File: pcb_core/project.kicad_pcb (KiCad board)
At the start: 2 copper layers, 212.3 x 91.7 mm, 145 parts, among them IC1 DRV8871DDA, IC10 DRV8871DDA, IC11 DRV8871DDA, IC12 DRV8871DDA, IC13 DRV8871DDA, IC14 DRV8871DDA, IC15 DRV8871DDA, IC16 DRV8871DDA, IC17 DRV8871DDA, IC18 DRV8871DDA, IC19 SX1509QBIULTRT, IC2 SX1509QBIULTRT, IC20 SI4214DDY-T1-GE3, IC3 DRV8871DDA, IC4 TCA9548APWR, IC5 DRV8871DDA, IC6 DRV8871DDA, IC7 DRV8871DDA, IC8 DRV8871DDA, IC9 DRV8871DDA, J1 Conn_01x02, J10 1053131103, J11 1053131103, J12 1053131103, J13 1053131103, J14 1053131103, J15 1053131103, J16 1053131103, J17 1053131103, J18 1053131103, J19 Conn_02x02_Counter_Clockwise, J2 1725656, J20 PCBConnector, J21 PCBConnector, J22 PCBConnector, J23 PCBConnector, J25 PCBConnector, J27 PCBConnector, J3 1053131103, J4 1053131103, J5 1053131103, J6 1053131103, J7 1053131103, J8 1053131103, J9 1053131103, U1 ESP32-S3-WROOM-2, U2 LTC4365TS8, U3 ESP32-DevKitC

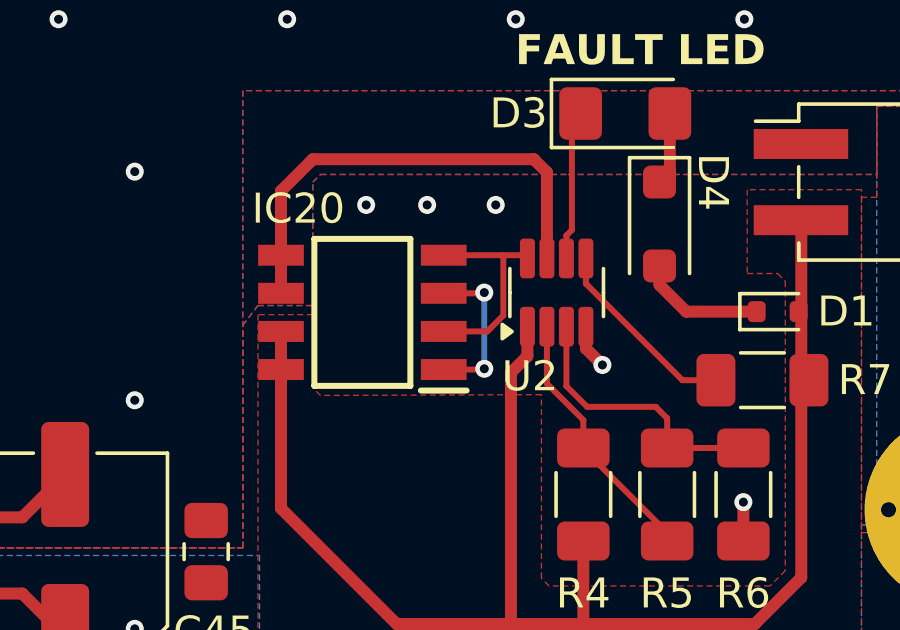
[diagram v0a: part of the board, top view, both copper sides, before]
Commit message: Optimize PCB to reduce vias
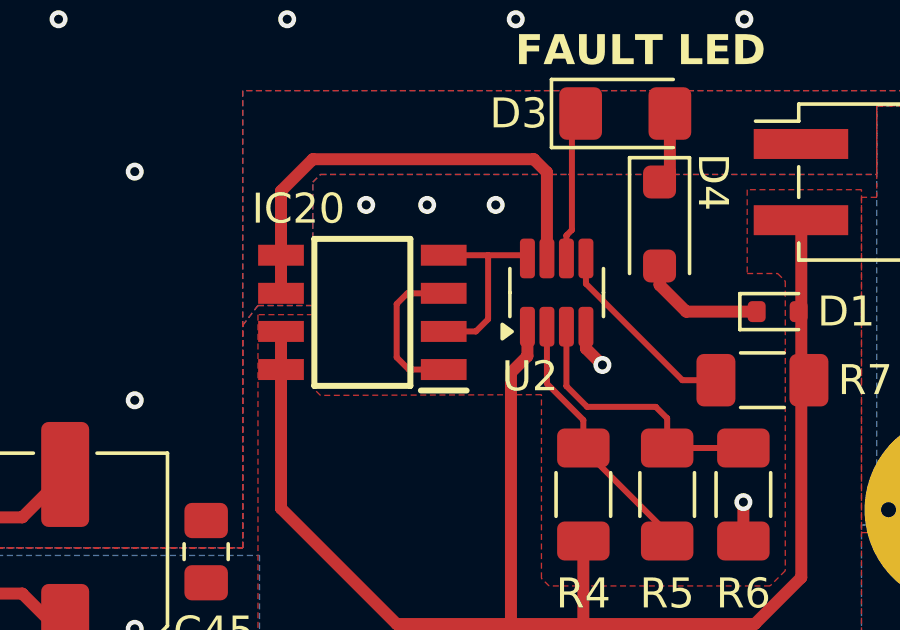
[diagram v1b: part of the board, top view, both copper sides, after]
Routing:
- net Net-(IC20-S1): track 5.19 -> 5.23 mm, vias 2 -> 0
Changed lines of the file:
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@@
 	)
 	(segment
-		(start 233.426 116.713)
-		(end 233.426 114.7064)
+		(start 232.918 116.84)
+		(end 232.918 114.7064)
 		(width 0.2)
 		(layer "F.Cu")
@@
 	)
 	(segment
-		(start 231.439 117.2464)
-		(end 232.8926 117.2464)
-		(width 0.2)
-		(layer "F.Cu")
-		(net 48)
-	)
-	(segment
-		(start 232.8926 117.2464)
-		(end 233.426 116.713)
+		(start 232.5116 117.2464)
+		(end 232.918 116.84)
 		(width 0.2)
 		(layer "F.Cu")
@@
 	)
 	(segment
-		(start 231.439 115.9764)
-		(end 232.7656 115.9764)
+		(start 231.439 117.2464)
+		(end 232.5116 117.2464)
+		(width 0.2)
+		(layer "F.Cu")
+		(net 48)
+	)
+	(segment
+		(start 230.2256 115.9764)
+		(end 229.87 116.332)
 		(width 0.2)
 		(layer "F.Cu")
@@
 	)
 	(segment
-		(start 231.439 118.5164)
-		(end 232.7656 118.5164)
+		(start 231.439 115.9764)
+		(end 230.2256 115.9764)
 		(width 0.2)
 		(layer "F.Cu")
 		(net 49)
 	)
-	(via
-		(at 232.791 118.491)
-		(size 0.6)
-		(drill 0.3)
-		(layers "F.Cu" "B.Cu")
-		(net 49)
-	)
-	(via
-		(at 232.791 115.951)
-		(size 0.6)
-		(drill 0.3)
-		(layers "F.Cu" "B.Cu")
+	(segment
+		(start 230.2764 118.5164)
+		(end 231.439 118.5164)
+		(width 0.2)
+		(layer "F.Cu")
 		(net 49)
 	)
 	(segment
-		(start 232.791 118.491)
-		(end 232.791 115.951)
+		(start 229.87 118.11)
+		(end 230.2764 118.5164)
 		(width 0.2)
-		(layer "B.Cu")
+		(layer "F.Cu")
 		(net 49)
 	)
+	(segment
+		(start 229.87 116.332)
+		(end 229.87 118.11)
+		(width 0.2)
+		(layer "F.Cu")
+		(net 49)
+	)

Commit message: Optimize PCB
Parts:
- moved J2 0.13 mm to (254.8, 122.9)
- moved J21 0.13 mm to (258.1, 116.3)
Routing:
- net GNDA: vias 367 -> 366
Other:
- outline, holes or cut-outs redrawn

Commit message: New package version of model train controller
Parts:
- removed C1, C11: 10uF, Capacitor_SMD:C_1206_3216Metric_Pad1.33x1.80mm_HandSolder
- removed C2, C3, C4: 0.1uF, Capacitor_SMD:C_1206_3216Metric_Pad1.33x1.80mm_HandSolder
- removed C43, C44, C8, C9: 0.1uF, Capacitor_SMD:C_0805_2012Metric_Pad1.18x1.45mm_HandSolder
- removed C45: 4.7uF, Capacitor_SMD:C_0805_2012Metric_Pad1.18x1.45mm_HandSolder
- removed C5: 1uF, Capacitor_SMD:C_1206_3216Metric_Pad1.33x1.80mm_HandSolder
- removed D1: 1N4148WT, Diode_SMD:D_SOD-523
- removed D3: RED LED, LED_SMD:LED_1206_3216Metric_Pad1.42x1.75mm_HandSolder
- removed D4: ~, Diode_SMD:D_SOD-123F
- removed IC19, IC2: SX1509QBIULTRT, library:QFN40P400X400X60-29N-D
- removed IC20: SI4214DDY-T1-GE3, library:SOIC127P600X175-8N
- removed IC4: TCA9548APWR, library:SOP65P640X120-24N
- removed J19: Conn_02x02_Counter_Clockwise, Connector_PinHeader_2.54mm:PinHeader_2x02_P2.54mm_Vertical_SMD
- removed J23: PCBConnector, TestPoint:TestPoint_THTPad_D3.0mm_Drill1.5mm
- removed R10, R11, R12, R16, R2, R9: 10k, Resistor_SMD:R_1206_3216Metric_Pad1.30x1.75mm_HandSolder
- removed R13, R14, R15, R17, R19, R20: 5k, Resistor_SMD:R_1206_3216Metric_Pad1.30x1.75mm_HandSolder
- removed R3: 0, Resistor_SMD:R_1206_3216Metric_Pad1.30x1.75mm_HandSolder
- removed R4: 250k, Resistor_SMD:R_1206_3216Metric_Pad1.30x1.75mm_HandSolder
- removed R5: 40.2k, Resistor_SMD:R_1206_3216Metric_Pad1.30x1.75mm_HandSolder
- removed R6: 13M, Resistor_SMD:R_1206_3216Metric_Pad1.30x1.75mm_HandSolder
- removed R7: 510k, Resistor_SMD:R_1206_3216Metric_Pad1.30x1.75mm_HandSolder
- removed S1, S2: EVP-3AA02Q, library:EVP3AA02Q
- removed S3: A6S-3102-PH, library:A6S3102PH
- removed U3: ESP32-DevKitC, PCM_Espressif:ESP32-DevKitC
- added U4: ~, cust_pcb:ioexpander, F.Cu at (175.5, 93.6)
- added U5: ~, cust_pcb:ioexpander, F.Cu at (87.4, 98.1)
- added U6: ~, cust_pcb:i2cmultiplexer, F.Cu at (117.3, 117.6)
- J1: value Conn_01x02 -> PCBConnector; footprint Connector_PinHeader_2.54mm:PinHeader_1x02_P2.54mm_Vertical -> TestPoint:TestPoint_THTPad_D3.0mm_Drill1.5mm
- U1: value ESP32-S3-WROOM-2 -> ~; footprint PCM_Espressif:ESP32-S3-WROOM-2 -> cust_pcb:esp32
- U2: value LTC4365TS8 -> ~; footprint Package_TO_SOT_SMD:TSOT-23-8 -> cust_pcb:voltage_protection
- moved J22 20.3 mm to (141.5, 128.8)
- moved J20 15.7 mm to (253.2, 100.6)
- moved J21 15.7 mm to (258.1, 100.6)
- moved J1 10.2 mm to (141.5, 123.7), turned to 0 degrees
- moved U2 8.44 mm to (233.4, 124.2), turned to 0 degrees
- moved U1 8.17 mm to (172.5, 116.1), turned to 0 degrees
- moved H6 2.54 mm to (154.9, 86.4)
- moved H7 2.54 mm to (154.9, 127.5)
- moved C42 0.28 mm to (218.7, 124.5), turned to -90 degrees
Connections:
- C42 pad 1: GNDA -> PROD_24V
- C42 pad 2: PROD_24V -> GNDA
- J1 pad 1: ESP32_TX -> ESP32_SCL
- J20 pad 1: /24V -> PROD_24V
- U1 pad 1: GNDD -> ESP32_SDA
- U1 pad 10: unconnected-(U1-GPIO17/U1TXD/ADC2_CH6-Pad10) -> GNDD
- U1 pad 11: unconnected-(U1-GPIO18/U1RXD/ADC2_CH7/CLK_OUT3-Pad11) -> GNDD
- U1 pad 12: unconnected-(U1-GPIO8/TOUCH8/ADC1_CH7/SUBSPICS1-Pad12) -> GNDD
- U1 pad 13: unconnected-(U1-GPIO19/U1RTS/ADC2_CH8/CLK_OUT2/USB_D--Pad13) -> GNDD
- U1 pad 14: unconnected-(U1-GPIO20/U1CTS/ADC2_CH9/CLK_OUT1/USB_D+-Pad14) -> GNDD
- U1 pad 15: unconnected-(U1-GPIO3/TOUCH3/ADC1_CH2-Pad15) -> GNDD
- U1 pad 16: unconnected-(U1-GPIO46-Pad16) -> GNDD
- U1 pad 17: unconnected-(U1-GPIO9/TOUCH9/ADC1_CH8/FSPIHD/SUBSPIHD-Pad17) -> GNDD
- U1 pad 18: unconnected-(U1-GPIO10/TOUCH10/ADC1_CH9/FSPICS0/FSPIIO4/SUBSPICS0-Pad18) -> VCC_3V3
- U1 pad 2: Net-(U1-3V3) -> ESP32_SCL
- U1 pad 3: /ESP32_EN -> GNDD
- U1 pad 4: unconnected-(U1-GPIO4/TOUCH4/ADC1_CH3-Pad4) -> GNDD
- U1 pad 5: unconnected-(U1-GPIO5/TOUCH5/ADC1_CH4-Pad5) -> GNDD
- U1 pad 6: unconnected-(U1-GPIO6/TOUCH6/ADC1_CH5-Pad6) -> GNDD
- U1 pad 7: unconnected-(U1-GPIO7/TOUCH7/ADC1_CH6-Pad7) -> GNDD
- U1 pad 8: unconnected-(U1-GPIO15/U0RTS/ADC2_CH4/XTAL_32K_P-Pad8) -> GNDD
- U1 pad 9: unconnected-(U1-GPIO16/U0CTS/ADC2_CH5/XTAL_32K_N-Pad9) -> GNDD
- U2 pad 1: VIN_24V -> GNDA
- U2 pad 2: Net-(U2-UV) -> GNDA
- U2 pad 3: Net-(U2-OV) -> GNDA
- U2 pad 4: GNDA -> PROD_24V
- U2 pad 5: Net-(U2-~{SHDN}) -> PROD_24V
- U2 pad 6: Net-(D3-K) -> PROD_24V
- U2 pad 7: PROD_24V -> /24V
- U2 pad 8: Net-(IC20-G1) -> /24V
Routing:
- net VCC_3V3: track 365.5 -> 167.9 mm, vias 20 -> 11
- net ESP32_TX: track 127.7 -> 0.00 mm
- net ESP32_RX: track 124.0 -> 0.00 mm
- net ESP32_SCL: track 124.4 -> 40.3 mm
- net ESP32_SDA: track 120.2 -> 42.4 mm, vias 1 -> 0
- net GNDD: track 64.9 -> 0.04 mm, vias 369 -> 354
- net VIN_24V: track 50.3 -> 0.00 mm
- net /ESP32_EN: track 42.6 -> 0.00 mm, vias 2 -> 0
- net IN2_13: track 14.5 -> 51.8 mm
- net IN1_13: track 14.9 -> 51.2 mm
- net IN2_14: track 24.2 -> 57.9 mm
- net IN1_14: track 25.6 -> 57.4 mm
- net IN2_9: track 43.7 -> 13.2 mm
- net IN1_9: track 41.5 -> 14.3 mm
- net IOEXP01_SCL: track 74.4 -> 49.0 mm, vias 2 -> 0
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- removed copper zone on F.Cu, net VIN_24V
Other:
- board text removed: "0x70 OFF OFF OFF 0x71 OFF OFF ON 0x72 OFF ON OFF 0x73 OFF ON ON 0x74 ON OFF OFF 0x75 ON OFF ON 0x76 ON ON OFF 0x77 ON ON ON"
- board text removed: "================"
- board text removed: "A0"
- board text removed: "A1"
- board text removed: "A2"
- board text removed: "ADDR A2 A1 A0"
- board text removed: "BOOT"
- board text removed: "Direct"
- board text removed: "FAULT LED"
- board text removed: "I²C Addresses:"
- board text removed: "I²C: 0x3E"
- board text removed: "Protected"
- board text removed: "RESET"
- board text removed: "RX"
- board text removed: "TX"
- board text removed: "UART"

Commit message: Add Panelize connector to PCB_Core
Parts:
- added T1: Tab, PCM_kikit:Tab, F.Cu at (61.0, 133.1)
- added T2: Tab, PCM_kikit:Tab, F.Cu at (157.5, 133.1)
- added T3: Tab, PCM_kikit:Tab, F.Cu at (247.9, 133.1)
- added T4: Tab, PCM_kikit:Tab, F.Cu at (47.8, 86.4)
- added T5: Tab, PCM_kikit:Tab, F.Cu at (261.1, 86.4)
- added T6: Tab, PCM_kikit:Tab, F.Cu at (61.0, 39.9)
- added T7: Tab, PCM_kikit:Tab, F.Cu at (157.5, 39.9)
- added T8: Tab, PCM_kikit:Tab, F.Cu at (247.9, 39.9)

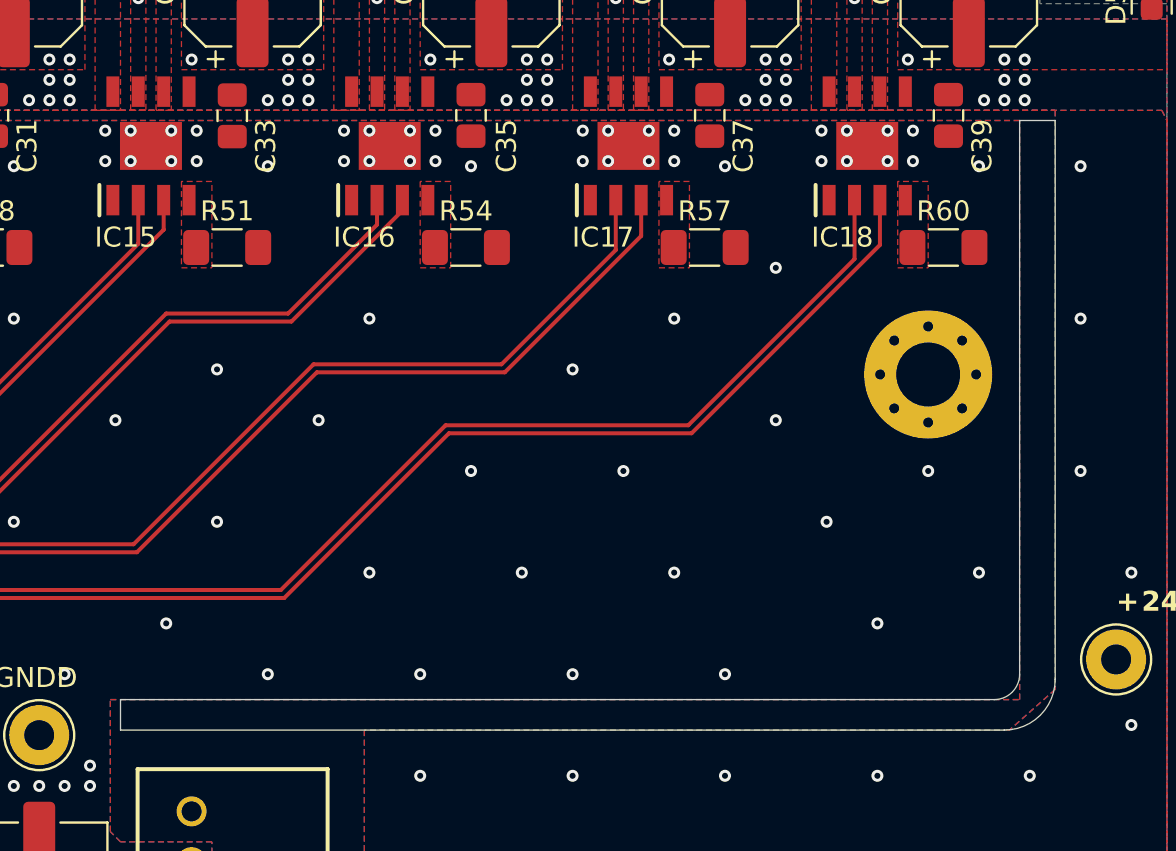
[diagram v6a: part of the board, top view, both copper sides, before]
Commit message: Optimize cutout rounding
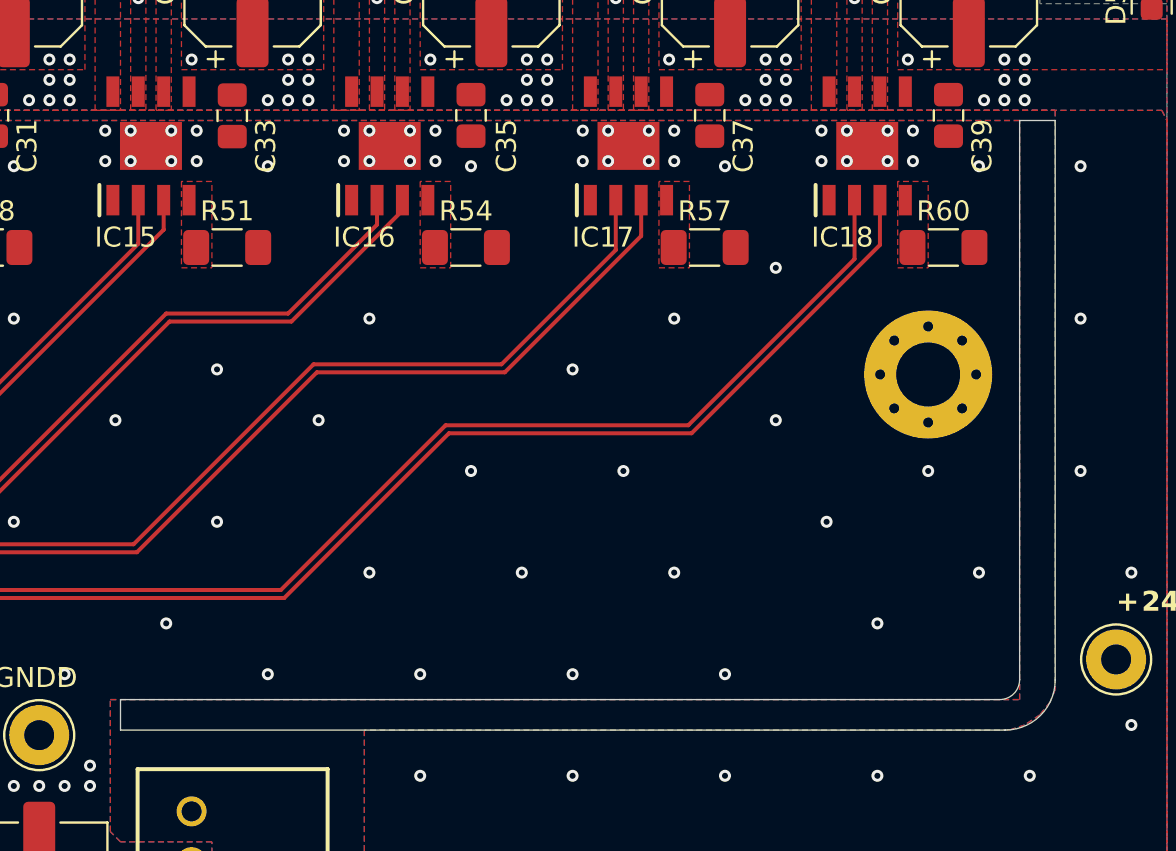
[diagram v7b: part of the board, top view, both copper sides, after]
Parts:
- moved T6 0.51 mm to (61.0, 40.4)
- moved T7 0.51 mm to (157.5, 40.4)
- moved T8 0.51 mm to (247.9, 40.4)
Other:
- outline, holes or cut-outs redrawn
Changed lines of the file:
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@@
 	(footprint "PCM_kikit:Tab"
 		(layer "F.Cu")
-		(at 157.48 39.878 -90)
+		(at 157.48 40.386 -90)
 		(descr "A symbol representing annotation for tab placement")
 		(property "Reference" "T7"
@@
 		)
 		(fp_text user "KIKIT: width: 3mm"
-			(at -5.5 0 360)
+			(at -5.5 0 0)
 			(layer "Dwgs.User")
 			(effects
@@
 		)
 		(fp_text user "KIKIT: width: 3mm"
-			(at -5.5 0 360)
+			(at -5.5 0 0)
 			(layer "Dwgs.User")
 			(effects
@@
 	(footprint "PCM_kikit:Tab"
 		(layer "F.Cu")
-		(at 60.96 39.878 -90)
+		(at 60.96 40.386 -90)
 		(descr "A symbol representing annotation for tab placement")
 		(property "Reference" "T6"
@@
 		)
 		(fp_text user "KIKIT: width: 3mm"
-			(at -5.5 0 360)
+			(at -5.5 0 0)
 			(layer "Dwgs.User")
 			(effects
@@
 		(descr "A symbol representing annotation for tab placement")
 		(property "Reference" "T5"
-			(at 0 -2 360)
+			(at 0 -2 0)
 			(layer "F.SilkS")
 			(hide yes)
@@
 		)
 		(property "Value" "Tab"
-			(at -2.75 -1 360)
+			(at -2.75 -1 0)
 			(layer "Dwgs.User")
 			(effects
@@
 		)
 		(property "Footprint" "PCM_kikit:Tab"
-			(at 0 0 360)
+			(at 0 0 0)
 			(layer "F.Fab")
 			(hide yes)
@@
 		)
 		(property "Datasheet" ""
-			(at 0 0 360)
+			(at 0 0 0)
 			(layer "F.Fab")
 			(hide yes)
@@
 		)
 		(property "Description" "KiKit tab annotations"
-			(at 0 0 360)
+			(at 0 0 0)
 			(layer "F.Fab")
 			(hide yes)
@@
 		)
 		(fp_text user "KIKIT: width: 3mm"
-			(at -5.5 0 360)
+			(at -5.5 0 0)
 			(layer "Dwgs.User")
 			(effects
@@
 		)
 		(fp_text user "KIKIT: width: 3mm"
-			(at -5.5 0 360)
+			(at -5.5 0 0)
 			(layer "Dwgs.User")
 			(effects
@@
 	(footprint "PCM_kikit:Tab"
 		(layer "F.Cu")
-		(at 247.904 39.878 -90)
+		(at 247.904 40.386 -90)
 		(descr "A symbol representing annotation for tab placement")
 		(property "Reference" "T8"
@@
 		)
 		(fp_text user "KIKIT: width: 3mm"
-			(at -5.5 0 360)
+			(at -5.5 0 0)
 			(layer "Dwgs.User")
 			(effects
@@
 		(layer "Edge.Cuts")
 	)
-	(gr_arc
-		(start 248.412 101.346)
-		(mid 248.040026 102.244025)
-		(end 247.142001 102.615999)
-		(stroke
-			(width 0.05)
-			(type default)
-		)
-		(layer "Edge.Cuts")
-	)
 	(gr_rect
 		(start 258.318 127.508)
@@
 		(layer "Edge.Cuts")
 	)
+	(gr_arc
+		(start 248.412 101.616)
+		(mid 248.119107 102.323107)
+		(end 247.412 102.616)
+		(stroke
+			(width 0.05)
+			(type default)
+		)
+		(layer "Edge.Cuts")
+	)
 	(gr_line
-		(start 247.65 104.14)
+		(start 247.69 104.14)
 		(end 203.454 104.14)
 		(stroke
@@
 	(gr_line
 		(start 248.412 73.66)
-		(end 248.412 101.346)
+		(end 248.412 101.616)
 		(stroke
 			(width 0.05)
@@
 	(gr_line
 		(start 203.454 102.616)
-		(end 247.142001 102.615999)
+		(end 247.412 102.616)
 		(stroke
 			(width 0.05)
@@
 		(layer "Edge.Cuts")
 	)
-	(gr_arc
-		(start 250.19 101.6)
-		(mid 249.446051 103.396051)
-		(end 247.65 104.14)
+	(gr_line
+		(start 250.19 73.66)
+		(end 250.19 101.64)
 		(stroke
 			(width 0.05)
@@
 		(layer "Edge.Cuts")
 	)
-	(gr_line
-		(start 250.19 73.66)
-		(end 250.19 101.6)
+	(gr_arc
+		(start 250.19 101.64)
+		(mid 249.457767 103.407767)
+		(end 247.69 104.14)
 		(stroke
 			(width 0.05)
@@
 		(polygon
 			(pts
-				(xy 58.928 68.58) (xy 58.928 73.152) (xy 250.19 73.152) (xy 250.19 102.108) (xy 247.904 104.14)
-				(xy 215.646 104.14) (xy 215.646 115.062) (xy 208.28 122.428) (xy 205.994 122.428) (xy 205.994 124.46)
-				(xy 215.646 124.46) (xy 225.806 124.46) (xy 225.806 114.808) (xy 226.06 114.554) (xy 255.778 114.554)
-				(xy 255.778 68.58)
+				(xy 58.928 68.58) (xy 58.928 73.152) (xy 250.19 73.152) (xy 250.19 102.108) (xy 249.936 102.743)
+				(xy 249.428 103.378) (xy 248.666 103.886) (xy 247.904 104.14) (xy 215.646 104.14) (xy 215.646 115.062)
+				(xy 208.28 122.428) (xy 205.994 122.428) (xy 205.994 124.46) (xy 215.646 124.46) (xy 225.806 124.46)
+				(xy 225.806 114.808) (xy 226.06 114.554) (xy 255.778 114.554) (xy 255.778 68.58)
 			)
 		)
